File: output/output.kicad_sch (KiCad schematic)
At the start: 25 parts, among them J3 Output, Q1 BSS138, Q2 BSS138, U1 OPA2990, U2 SN74LVC1G3157, U3 INA2181, U4 SN74LVC1G3157

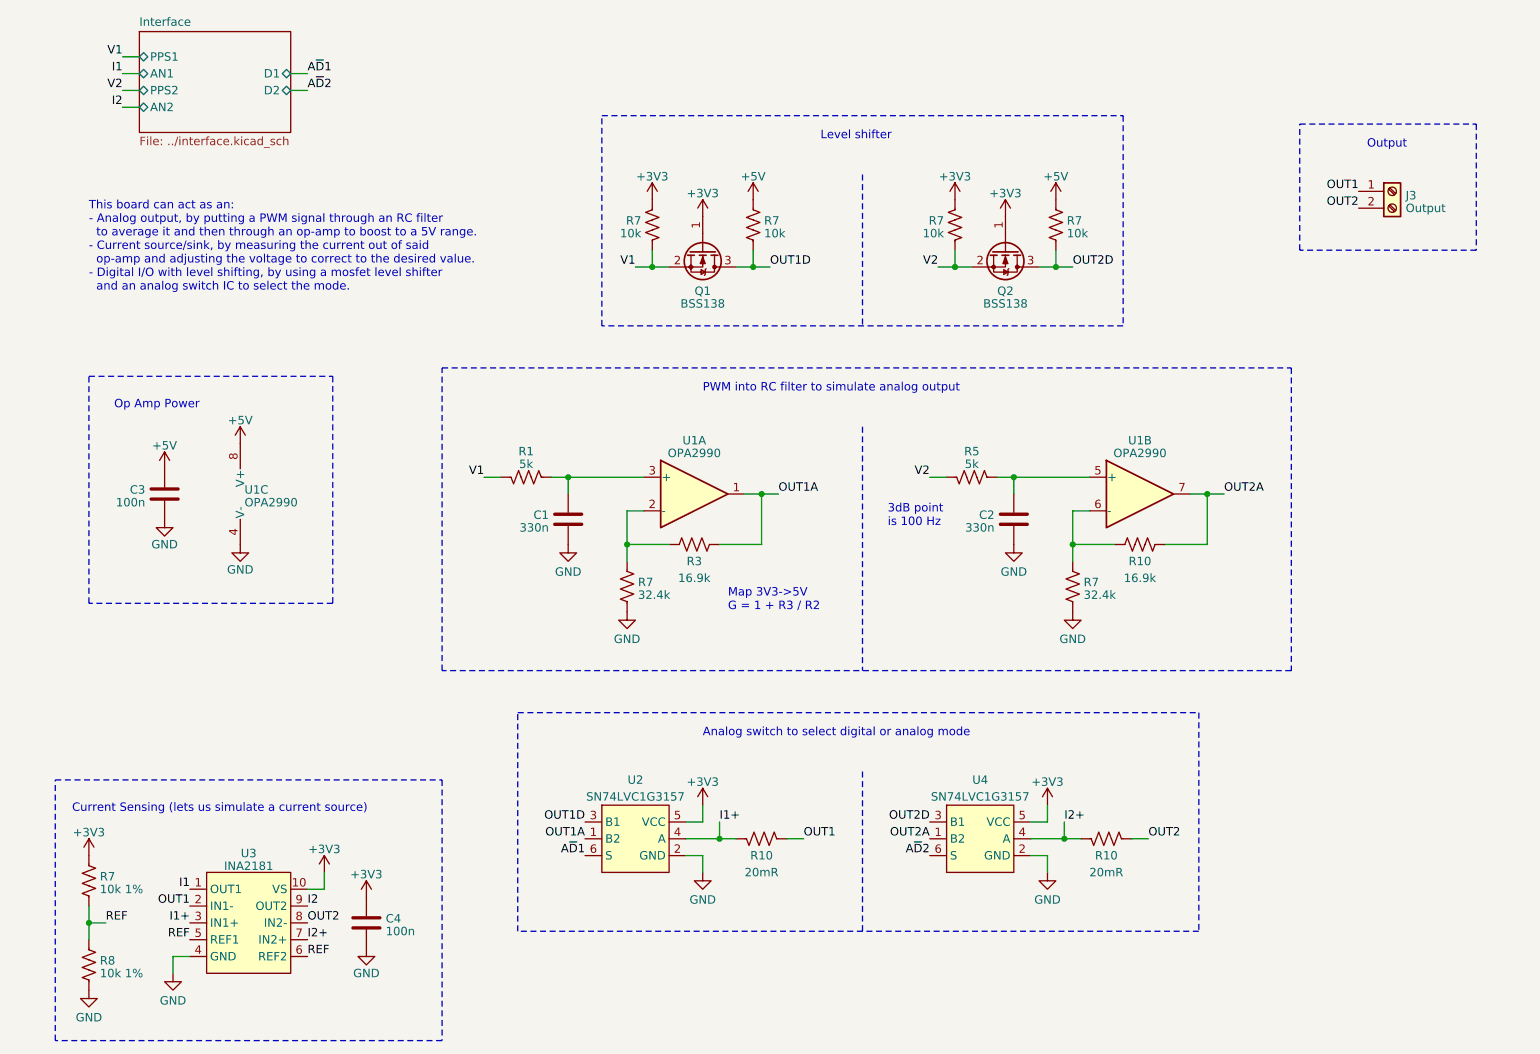
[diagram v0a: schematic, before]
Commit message: Address review comments, finish routing HILT main board
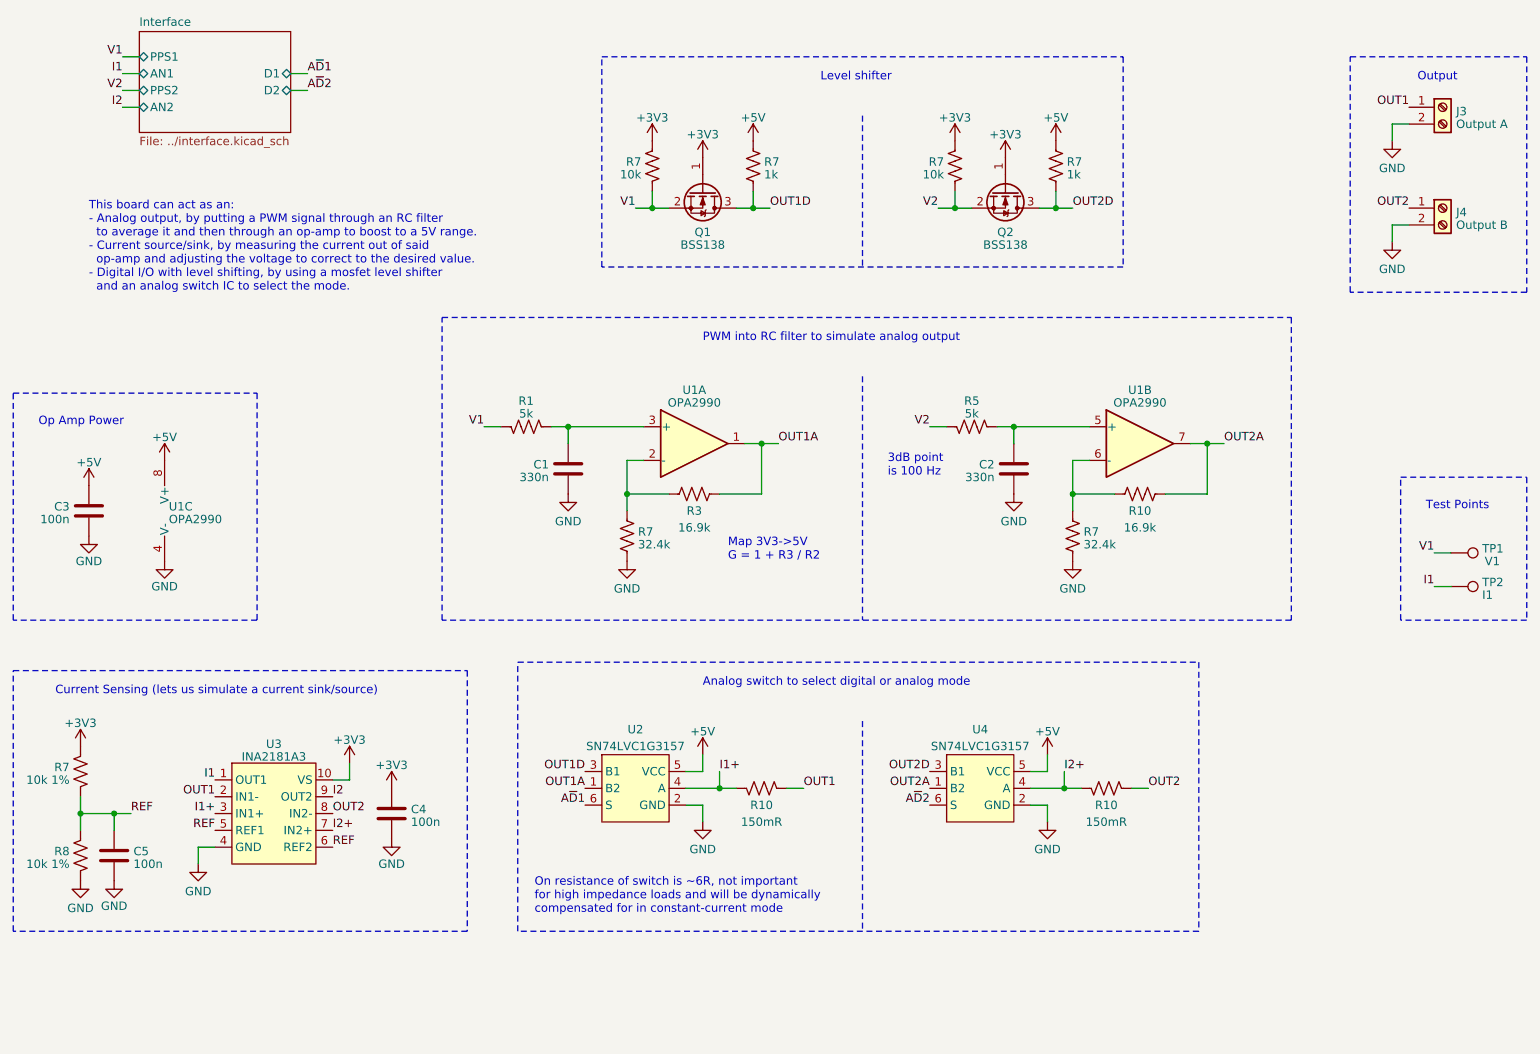
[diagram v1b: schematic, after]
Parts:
- added C5: 100n, Capacitor_SMD:C_0805_2012Metric_Pad1.18x1.45mm_HandSolder, symbol Device:C
- added J4: Output B, TerminalBlock_Phoenix:TerminalBlock_Phoenix_PT-1,5-2-3.5-H_1x02_P3.50mm_Horizontal, symbol Connector:Screw_Terminal_01x02
- added TP1: V1, TestPoint:TestPoint_Pad_D1.0mm, symbol Connector:TestPoint
- added TP2: I1, TestPoint:TestPoint_Pad_D1.0mm, symbol Connector:TestPoint
- J3: value Output -> Output A; footprint TerminalBlock_Phoenix:TerminalBlock_Phoenix_PT-1,5-2-5.0-H_1x02_P5.00mm_Horizontal -> TerminalBlock_Phoenix:TerminalBlock_Phoenix_PT-1,5-2-3.5-H_1x02_P3.50mm_Horizontal
- R10: value 20mR -> 150mR
- R7: value 10k -> 1k
- U3: value INA2181 -> INA2181A3
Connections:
- net +3V3: no longer U2.5 (VCC), U4.5 (VCC)
- net +5V: now also U2.5 (VCC), U4.5 (VCC)
- net GND: now also J3.2 (Pin_2), C5.2, J4.2 (Pin_2)
- net I1: now also TP2.1
- net OUT2: now also J4.1 (Pin_1); no longer J3.2 (Pin_2)
- net REF: now also C5.1
- net V1: now also TP1.1
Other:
- note added: "Current Sensing (lets us simulate a current sink/source)"
- note added: "On resistance of switch is ~6R, not important for high impedance loads and will be dynamically compensated for in constant-current mode"
- note added: "Test Points"
- note removed: "Current Sensing (lets us simulate a current source)"
- moved on the sheet: C1, C2, C3, C4, J3, Q1, Q2, R1, R10, R3, R5, R7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
